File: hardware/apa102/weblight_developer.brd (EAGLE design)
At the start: 43.2 x 12 mm, 14 parts, among them U1 ATTiny85-20SU

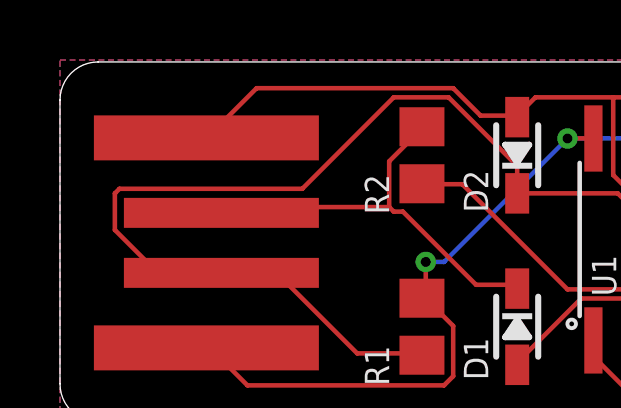
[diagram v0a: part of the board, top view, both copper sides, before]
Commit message: Separate LED type and adopt new board versioning scheme
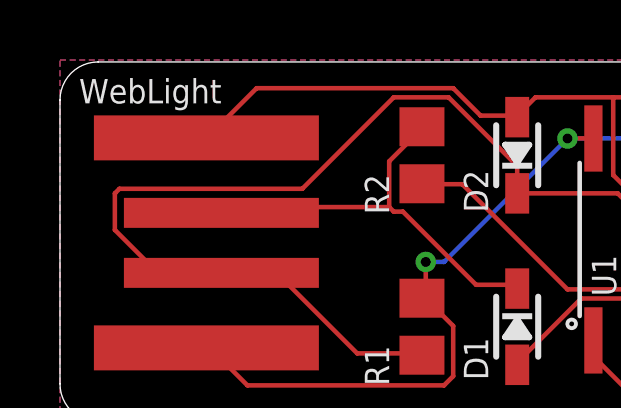
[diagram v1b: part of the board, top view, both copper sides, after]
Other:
- board text added: "WebLight"
- board text added: "a-osh1"
- board text removed: "Version osh4"
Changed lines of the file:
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@@
 <wire x1="41.91" y1="12" x2="1.27" y2="12" width="0" layer="20"/>
 <wire x1="1.27" y1="12" x2="0" y2="10.73" width="0" layer="20" curve="90"/>
-<text x="42.545" y="2.54" size="0.8128" layer="22" font="vector" rot="MR0">Version osh4</text>
+<text x="42.545" y="2.54" size="0.8128" layer="22" font="vector" rot="MR0">a-osh1</text>
 <polygon width="0.4064" layer="43">
 <vertex x="0" y="12.065"/>
@@
 <text x="42.545" y="1.27" size="0.8128" layer="22" font="vector" rot="MR0">github.com/sowbug/weblight</text>
 <rectangle x1="24.765" y1="1.27" x2="42.545" y2="3.175" layer="43"/>
+<text x="0.635" y="11.43" size="0.8128" layer="21" font="vector" align="top-left">WebLight</text>
 </plain>
 <attributes>
